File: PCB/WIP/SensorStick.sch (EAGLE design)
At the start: 89 parts, among them U1 TPD4F003DQDR, U10 LIS3MDLTR, U11 LIS3MDLTR, U2 BMI088, U3 BMI088, U4 BMI088, U5 STM32H743ZIT6, U9 LIS3MDLTR, Y1 ECS-TXO-3225MV-400-TR

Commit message: fixing connections XD
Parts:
- added R22, R25: 0, SparkFun-Resistors:0OHM-0603-1/10W-5%
- added R23, R24: 22, SparkFun-Resistors:22OHM-0402-1/10W-1%
- C24, C25, C27, C28, C29, C30, C31, C32, C33: value (none) -> 0.1uf
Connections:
- removed net PDR_ON: U5G$1.PDR_ON
- removed net TRACESWO: U5G$2.PB3(JTDO/TRACESWO)
- new net EXTI0_1: R23.2, U2.INT1
- new net EXTI1: U3.INT1
- new net EXTI1_1: R24.2, U2.INT3
- new net GPIO_EXTI0_1: R23.1, U5G$4.PG0
- new net GPIO_EXTI1_1: R24.1, U5G$4.PG1
- new net IMU_INT1: R22.1, U3.INT2
- new net IMU_INT3: R22.2, U3.INT4
- new net IMU_INT5: R25.1, U2.INT2
- new net IMU_INT6: R25.2, U2.INT4
- new net N$15: R19.1, U5G$3.PE7
- new net N$16: R20.1, U5G$3.PE8
- new net N$17: R21.1, U5G$3.PE9
- net 3V3: now also L1.2, U5G$1.PDR_ON, U5G$1.VSSA; no longer L1.1
- net EXTI0: no longer U2.INT1, U3.INT1
- net EXTI2: no longer U2.INT3, U3.INT3
- net EXTI3: now also U3.INT3
- net IMU_INT2: no longer U2.INT2, U3.INT2
- net IMU_INT4: no longer U2.INT4, U3.INT4
- net SWO: now also U5G$2.PB3(JTDO/TRACESWO)
- net VREF: now also L1.1; no longer L1.2

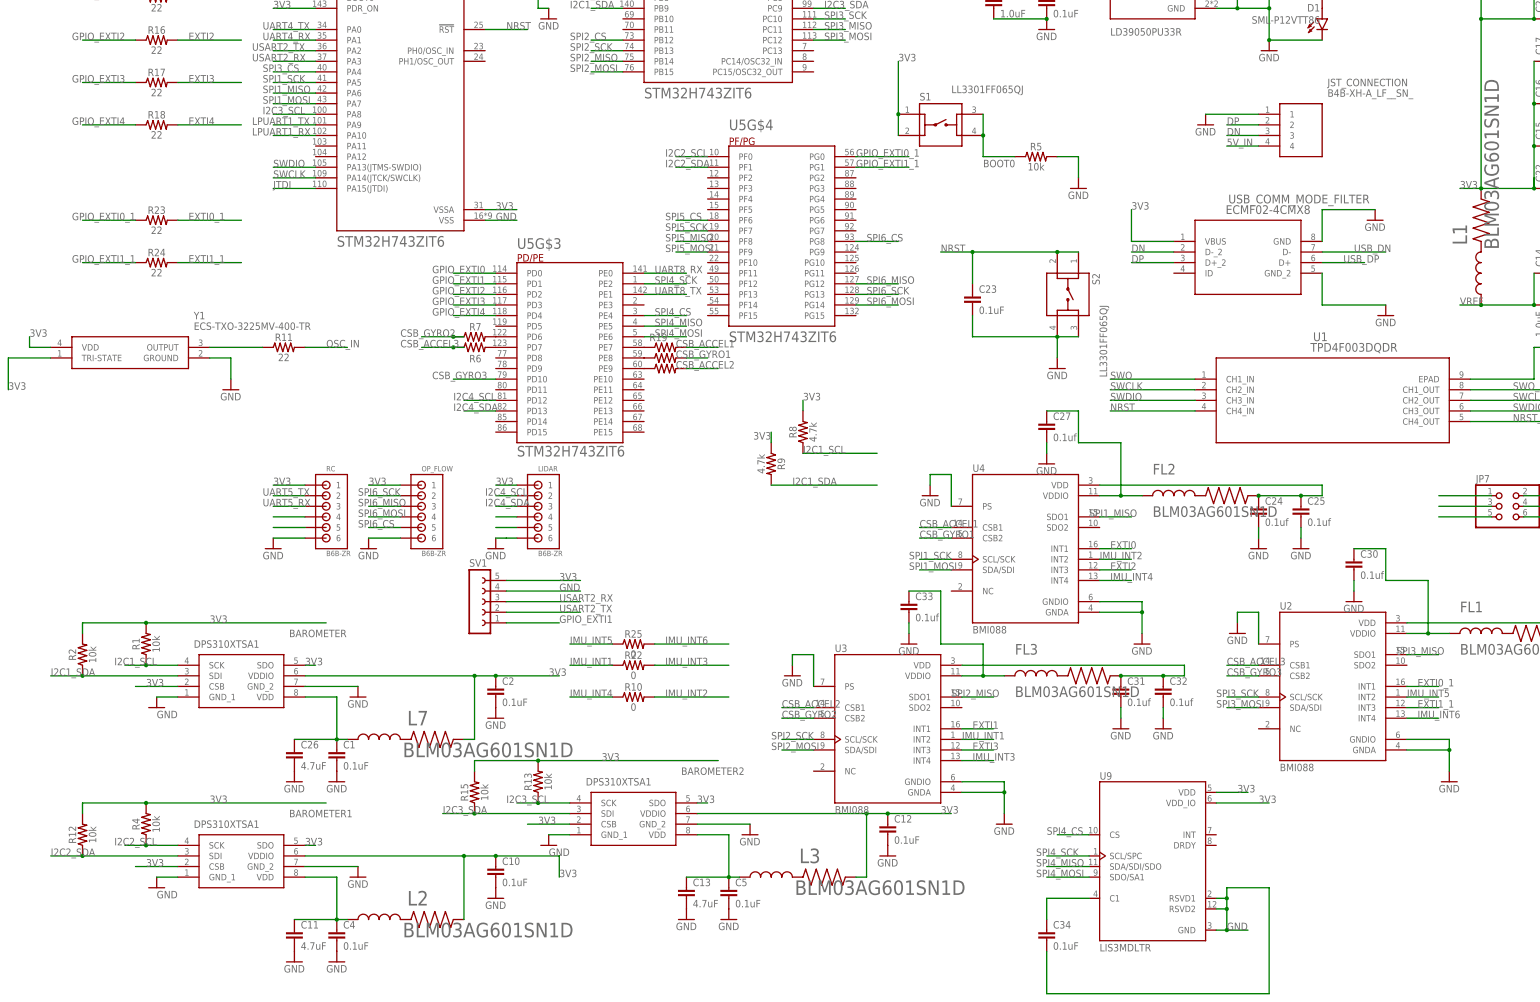
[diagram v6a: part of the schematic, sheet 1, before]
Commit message: rearranged everything again and grouped relevant components together, still a lot of clearance errors when wiring
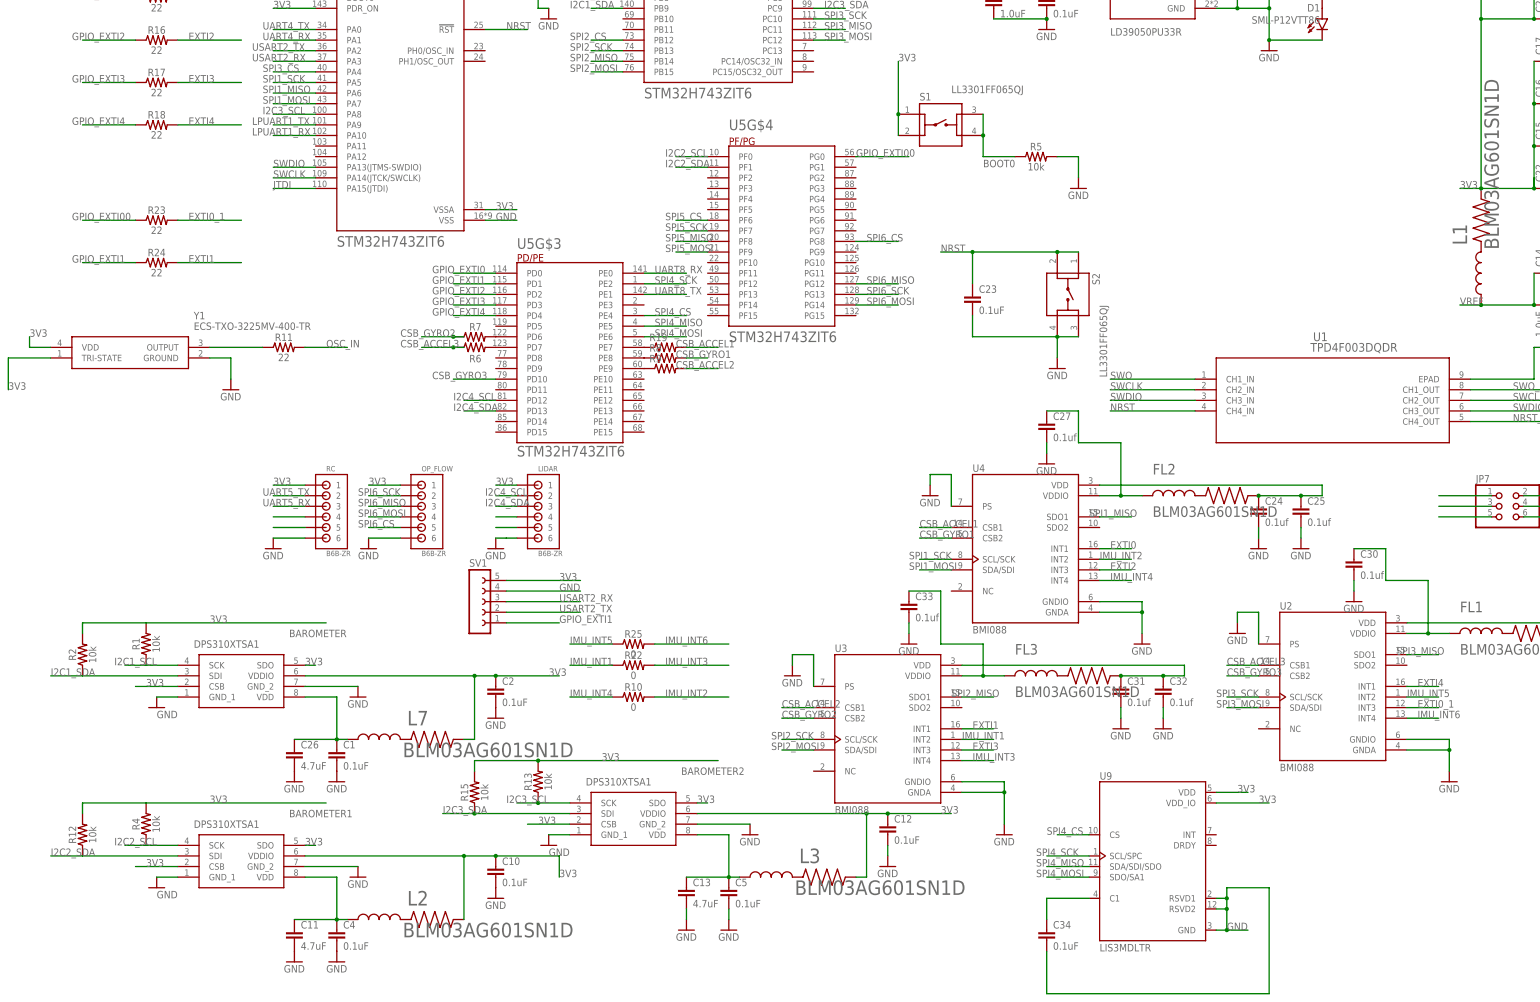
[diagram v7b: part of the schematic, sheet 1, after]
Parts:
- removed JST_CONNECTION: B4B-XH-A_LF__SN_, B4B-XH-A_LF__SN_:B4B-XH-A_LF__SN_
- removed R20, R21: RT0402FRE07220RL, ce-capstone:RT0402FRE07220RL
- removed USB_COMM_MODE_FILTER: ECMF02-4CMX8, ECMF02-4CMX8:ECMF02-4CMX8
- R8, R9: value 4.7k -> RT0402FRE07220RL; device SparkFun-Resistors:4.7KOHM-0603-1/10W-1% -> ce-capstone:RT0402FRE07220RL
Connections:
- net GPIO_EXTI0_1 renamed GPIO_EXTI00
- removed net DN: JST_CONNECTION.3, USB_COMM_MODE_FILTER.D-_2
- removed net DP: JST_CONNECTION.2, USB_COMM_MODE_FILTER.D+_2
- removed net EXTI1_1: R24.2, U2.INT3
- removed net GPIO_EXTI1_1: R24.1, U5G$4.PG1
- removed net USB_DN: USB_COMM_MODE_FILTER.D-
- removed net USB_DP: USB_COMM_MODE_FILTER.D+
- net 3V3: no longer R8.2, R9.1, USB_COMM_MODE_FILTER.VBUS
- net 5V_IN: no longer JST_CONNECTION.4
- net CSB_ACCEL2: now also R9.2; no longer R21.2
- net CSB_GYRO1: now also R8.2; no longer R20.2
- net EXTI0_1: now also U2.INT3; no longer U2.INT1
- net EXTI1: now also R24.2
- net EXTI4: now also U2.INT1
- net GND: no longer JST_CONNECTION.1, USB_COMM_MODE_FILTER.GND, USB_COMM_MODE_FILTER.GND_2
- net GPIO_EXTI1: now also R24.1
- net I2C1_SCL: no longer R8.1
- net I2C1_SDA: no longer R9.2
- net N$16: now also R8.1; no longer R20.1
- net N$17: now also R9.1; no longer R21.1
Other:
- moved on the sheet: R8, R9

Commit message: first draft pretty much
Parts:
- removed JP7: (no value), pinhead:PINHD-2X3
- C24, C25, C27, C28, C29, C30, C31, C32, C33: value 0.1uf -> 0.1uF; device capacitor-wima:C2.5/4 -> SparkFun-Capacitors:0.1UF-0603-25V-5%
- C3, C34, C35, C36: device capacitor-wima:C2.5/4 -> SparkFun-Capacitors:0.1UF-0603-25V-5%
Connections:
- removed net SWCLK_O1: JP7.3
- removed net SWDIO_O1: JP7.5
- removed net SWO_O1: JP7.1
- removed net USART1_RX: JP7.4
- removed net USART1_TX: JP7.2
- net 3V2: now also C28.2, C29.2; no longer C28.1, C29.1
- net 3V3: now also C3.2; no longer C3.1
- net 3V4: now also C24.2, C25.2; no longer C24.1, C25.1
- net 3V5: now also C31.2, C32.2; no longer C31.1, C32.1
- net GND: now also C24.1, C25.1, C27.1, C28.1, C29.1, C3.1, C30.1, C31.1, C32.1, C33.1, C34.1, C35.1, C36.1; no longer C24.2, C25.2, C27.2, C28.2, C29.2, C3.2, C30.2, C31.2, C32.2, C33.2, C34.2, C35.2, C36.2
- net N$10: now also C33.2; no longer C33.1
- net N$11: now also C36.2; no longer C36.1
- net N$4: now also C34.2; no longer C34.1
- net N$7: now also C35.2; no longer C35.1
- net N$8: now also C27.2; no longer C27.1
- net N$9: now also C30.2; no longer C30.1
- net NRST_O: no longer JP7.6
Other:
- moved on the sheet: C24, C25, C27, C28, C29, C3, C30, C31, C32, C33, C34, C35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
